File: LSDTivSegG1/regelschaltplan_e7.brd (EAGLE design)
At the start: 160 x 100 mm, 90 parts, among them IC1 LF33AB, IC3 MAX232, IC4 MEGA32-P, Q2 BS170, Q3 BS170, Q4 BS170, Q5 BS170, Q6 BS170, Q7 BS170, Q8 BS170

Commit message: edit regellayout done
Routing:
- net DIRL_CTL: track 199.6 -> 186.2 mm
- net RS232TX_CON: track 71.8 -> 67.3 mm
- net BAT_PWM_CTL: track 183.2 -> 181.8 mm
- net RS232RX: track 70.1 -> 69.3 mm
- net ACCEL_X: track 138.3 -> 137.5 mm
- net 5V_LST: track 133.8 -> 133.1 mm
- net N$12: track 14.0 -> 13.3 mm
- net +3V3: track 246.1 -> 245.4 mm
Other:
- board text added: "1"
- board text added: "2"
- board text added: "3"
- board text added: "3.3V"
- board text added: "5V"
- board text added: "BAT_PWM"
- board text added: "DIR_L"
- board text added: "DIR_R"
- board text added: "ENABLE"
- board text added: "MOTOR_L"
- board text added: "MOTOR_R"
- board text removed: "MOTOR 1"
- board text removed: "TEXT"

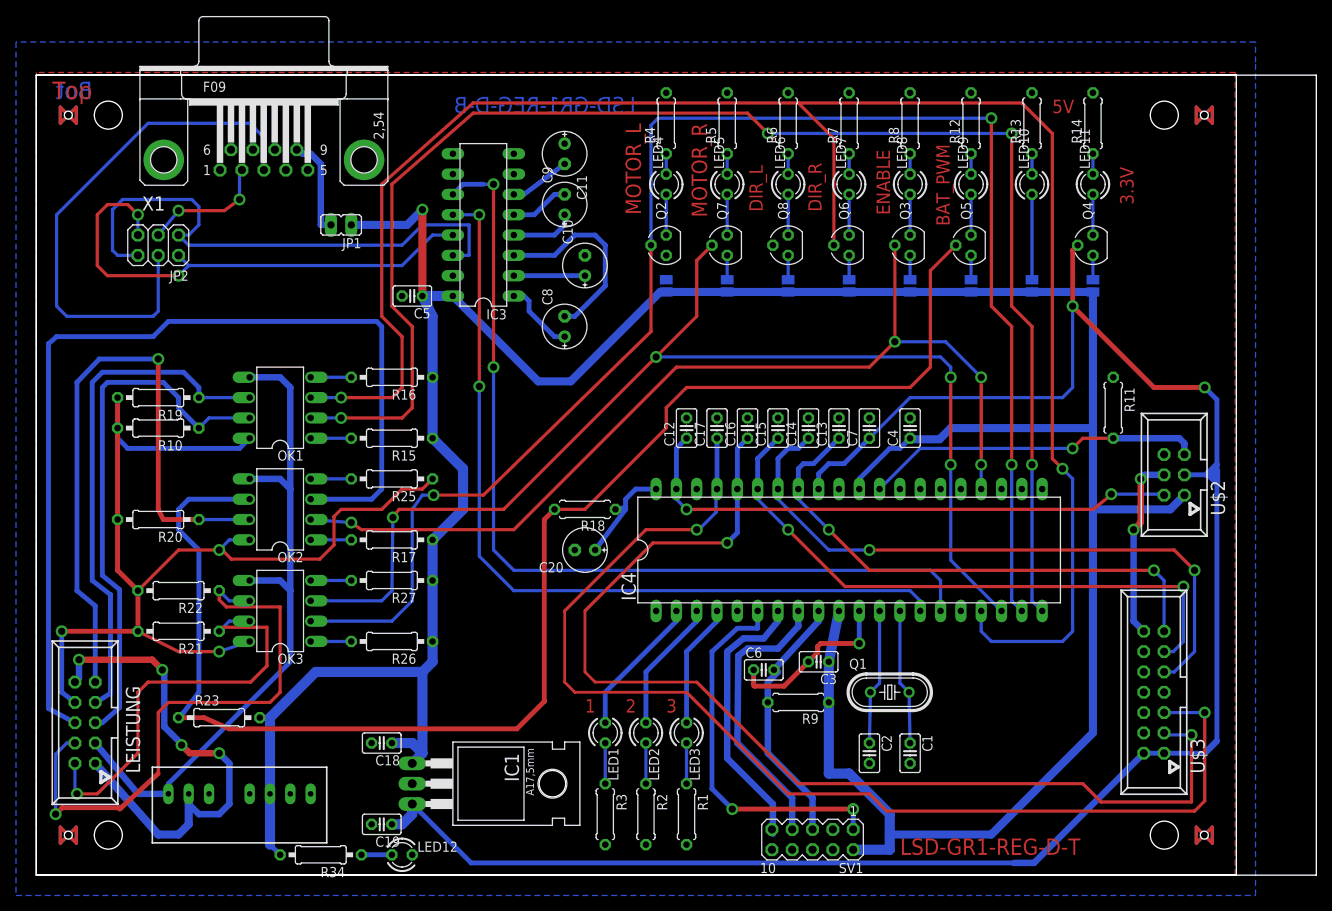
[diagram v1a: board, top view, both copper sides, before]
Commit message: edit  regelschaltplan_e7 bauteil fixed
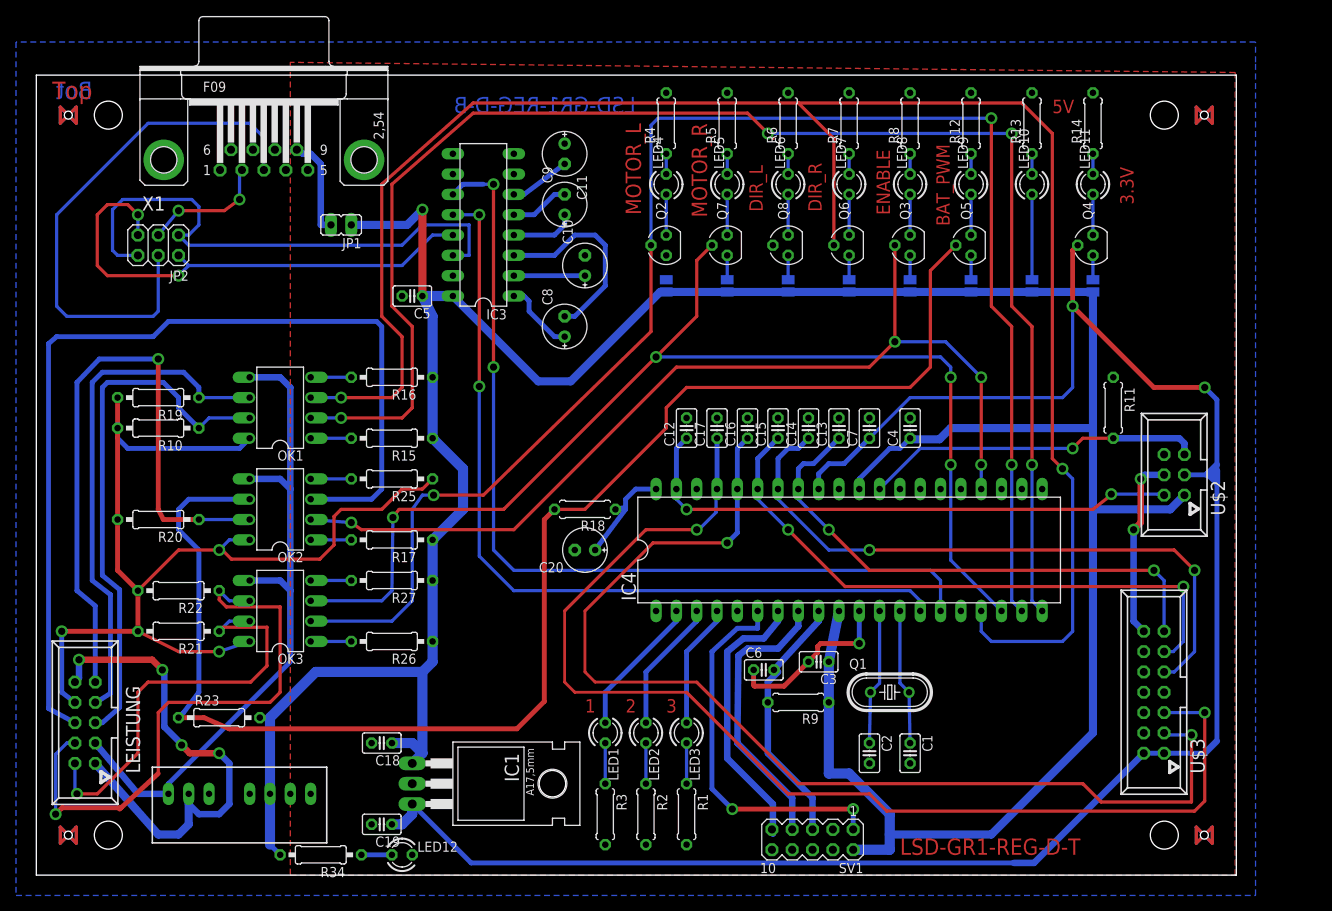
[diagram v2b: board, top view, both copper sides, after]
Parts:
- DC1: device traco_tmr:TRACO_SIP-8 -> regelschaltplan_e7:TRACO_SIP-8
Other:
- board size 160 x 100 mm -> 150 x 100 mm
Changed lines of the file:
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@@
 <setting verticaltext="up"/>
 </settings>
-<grid distance="50" unitdist="mil" unit="mil" style="lines" multiple="1" display="no" altdistance="20" altunitdist="mil" altunit="mil"/>
+<grid distance="50" unitdist="mil" unit="mm" style="lines" multiple="1" display="no" altdistance="20" altunitdist="mil" altunit="mm"/>
 <layers>
 <layer number="1" name="Top" color="4" fill="1" visible="yes" active="yes"/>
@@
 <layer number="43" name="vRestrict" color="2" fill="10" visible="yes" active="yes"/>
 <layer number="44" name="Drills" color="7" fill="1" visible="no" active="yes"/>
-<layer number="45" name="Holes" color="7" fill="1" visible="no" active="yes"/>
+<layer number="45" name="Holes" color="7" fill="1" visible="yes" active="yes"/>
 <layer number="46" name="Milling" color="3" fill="1" visible="no" active="yes"/>
 <layer number="47" name="Measures" color="7" fill="1" visible="no" active="yes"/>
@@
 <board>
 <plain>
-<wire x1="0" y1="0" x2="160" y2="0" width="0" layer="20"/>
-<wire x1="160" y1="0" x2="160" y2="100" width="0" layer="20"/>
-<wire x1="160" y1="100" x2="0" y2="100" width="0" layer="20"/>
-<wire x1="0" y1="100" x2="0" y2="0" width="0" layer="20"/>
 <text x="73.66" y="93.98" size="1.9304" layer="1" font="vector" ratio="21" rot="R270">MOTOR_L</text>
 <text x="81.915" y="93.98" size="1.9304" layer="1" font="vector" ratio="21" rot="R270">MOTOR_R</text>
@@
 <param name="mdSmdStop" value="0mil"/>
 <param name="msWidth" value="14mil"/>
-<param name="msDrill" value="24mil"/>
+<param name="msDrill" value="0.8mm"/>
 <param name="msMicroVia" value="9.99mm"/>
 <param name="msBlindViaRatio" value="0.5"/>
@@
 <element name="R26" library="rcl" package="0207/10" value="330" x="44.45" y="29.21" rot="R180"/>
 <element name="R27" library="rcl" package="0207/10" value="330" x="44.45" y="36.83" rot="R180"/>
-<element name="DC1" library="traco_tmr" package="TRACO_SIP-8" value="TMR" x="25.4" y="10.16"/>
+<element name="DC1" library="regelschaltplan_e7" package="TRACO_SIP-8" value="TMR" x="25.4" y="10.16"/>
 <element name="LED12" library="led" package="LED3MM" value="blau" x="45.72" y="2.54"/>
 <element name="R34" library="rcl" package="0207/10" value="100" x="35.56" y="2.54" rot="R180"/>
@@
 <wire x1="137.16" y1="31.75" x2="138.43" y2="30.48" width="0.8128" layer="16"/>
 <polygon width="0.6096" layer="1">
-<vertex x="0" y="0"/>
+<vertex x="31.75" y="0"/>
 <vertex x="149.86" y="0"/>
 <vertex x="149.86" y="100.33"/>
-<vertex x="0" y="100.33"/>
+<vertex x="31.75" y="101.6"/>
 </polygon>
 </signal>
@@
 </signal>
 </signals>
+<errors>
+</errors>
 </board>
 </drawing>
